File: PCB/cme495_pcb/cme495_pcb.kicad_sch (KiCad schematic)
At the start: 13 parts, among them J1 Conn_01x20_Socket, J2 Conn_01x20_Socket, J3 Conn_01x05_Socket, J4 Conn_01x05_Socket, J5 Conn_01x05_Socket, J6 Conn_01x05_Socket, J7 Conn_01x12_Socket, SW0 SW_Push_Open, SW1 SW_Push_Open, SW2 SW_Push_Open, SW3 SW_Push_Open, U1 MCP3208, U2 MCP3208

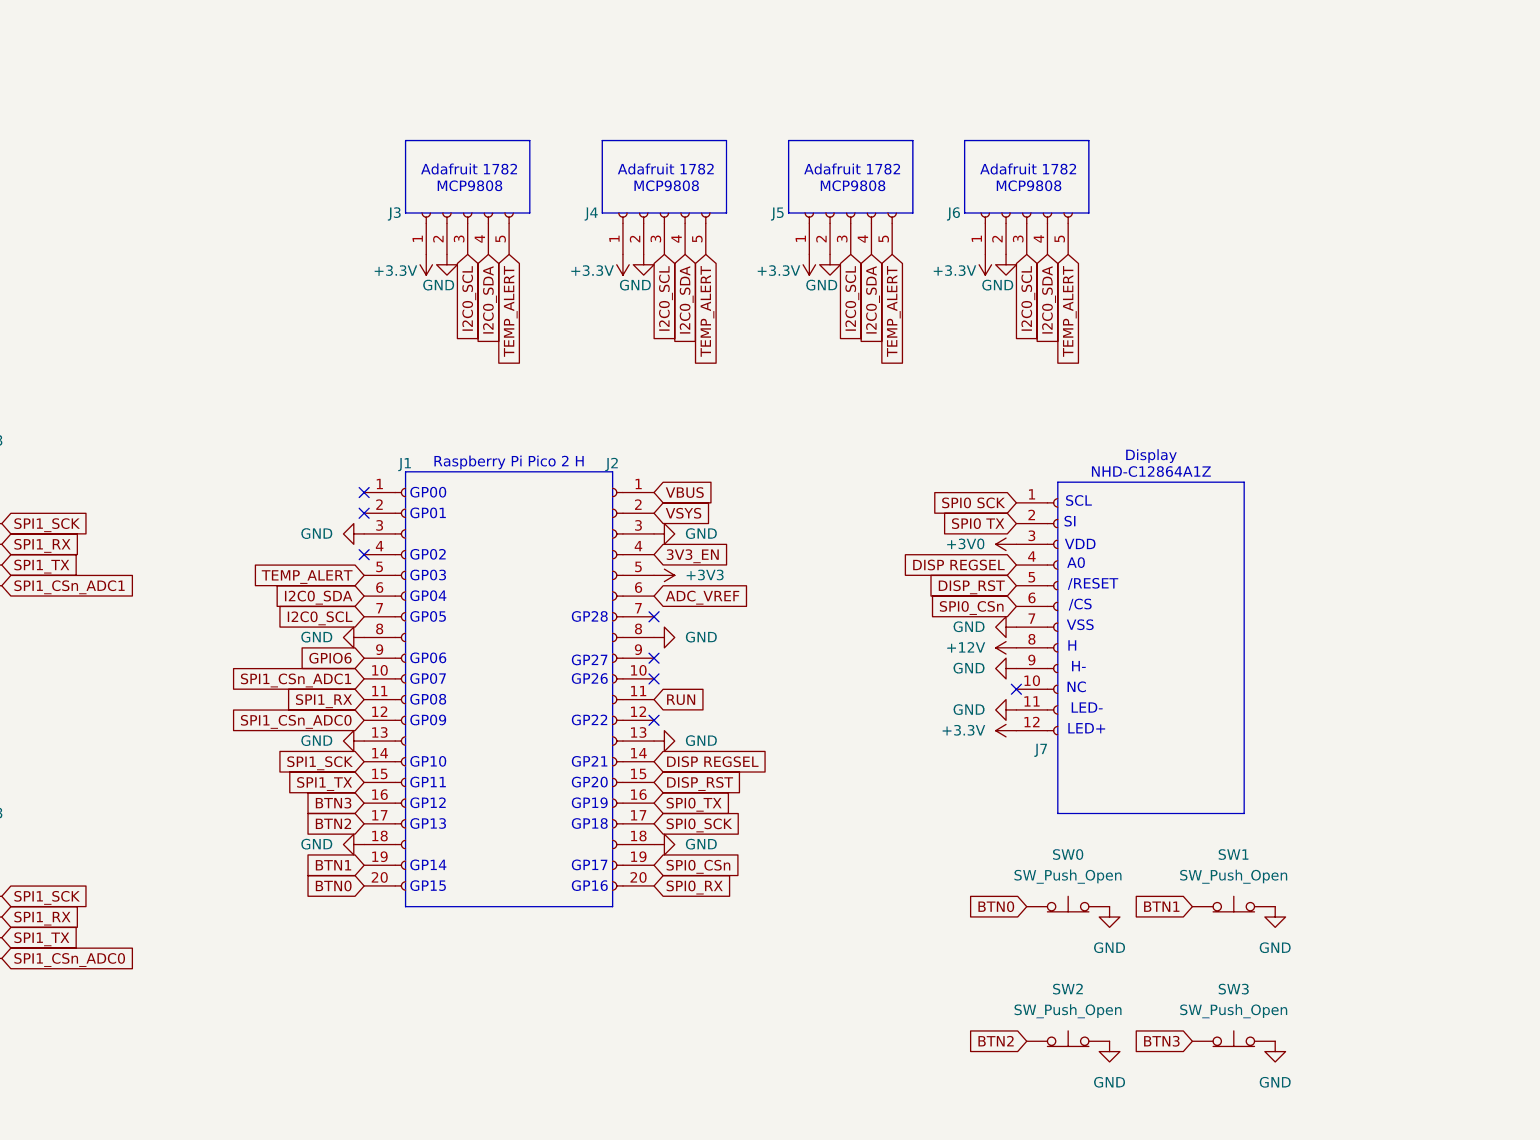
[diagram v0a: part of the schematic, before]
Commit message: added xh connector plans
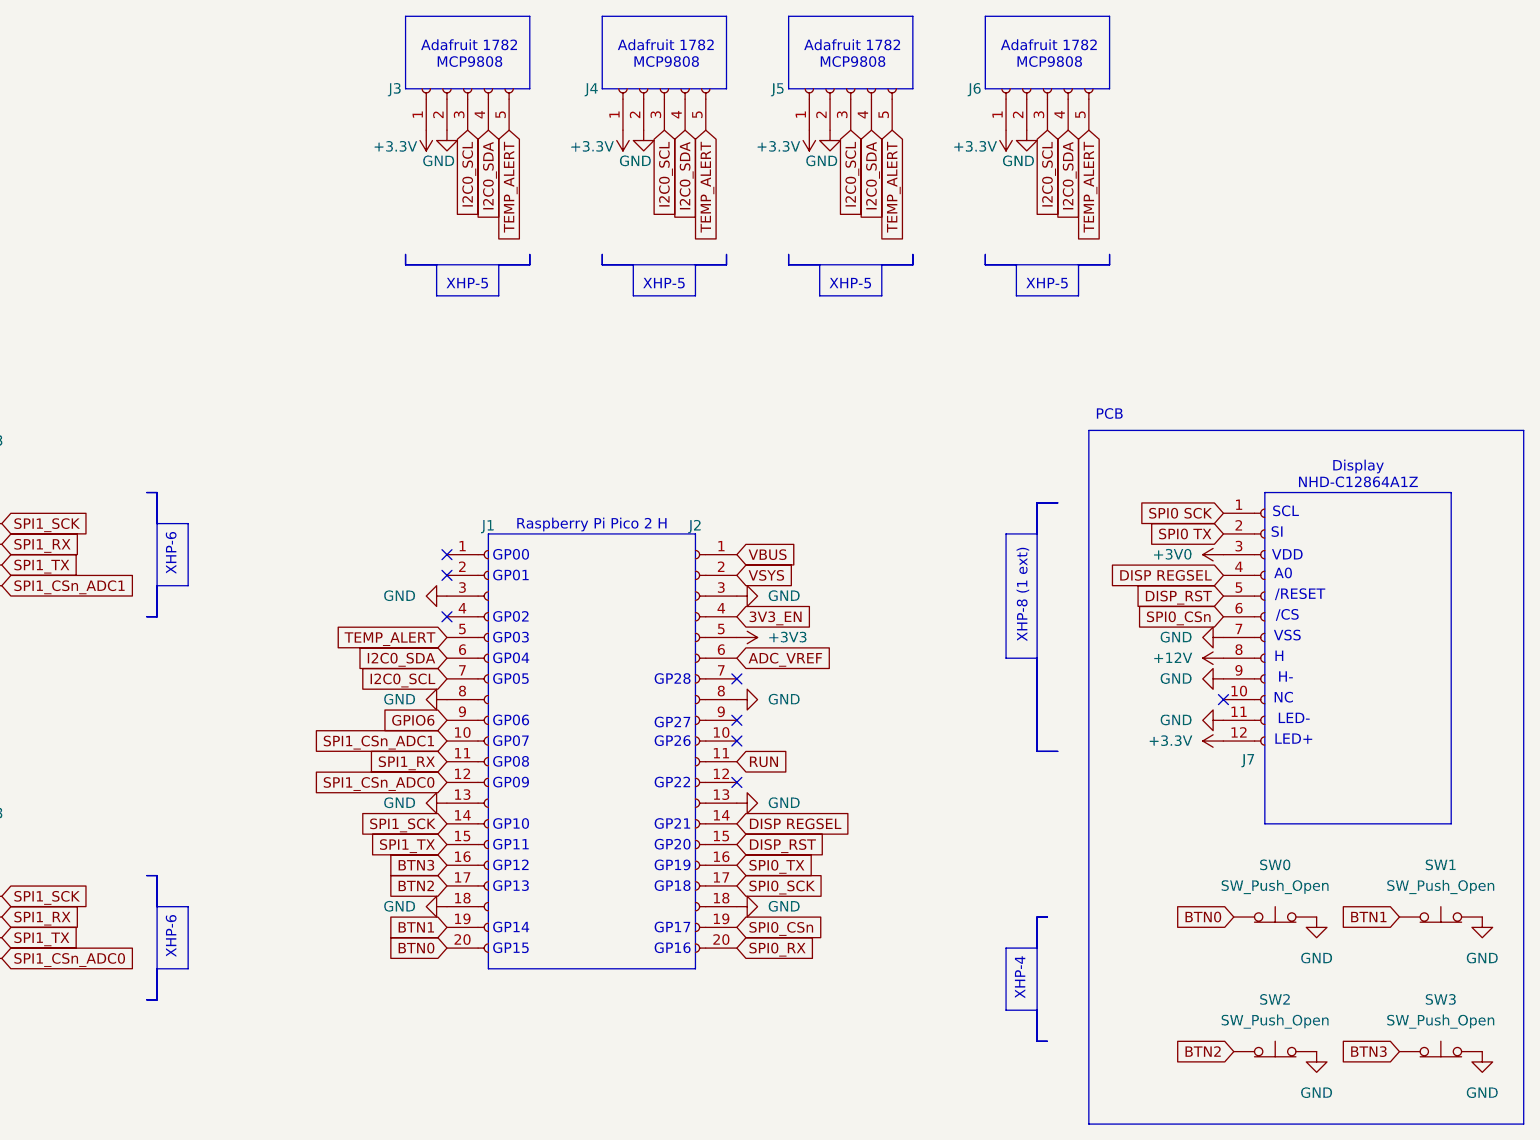
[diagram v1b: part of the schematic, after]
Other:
- note added: "PCB"
- note added: "XHP-4"
- note added: "XHP-5"
- note added: "XHP-6"
- note added: "XHP-8 (1 ext)"
- moved on the sheet: J1, J2, J3, J4, J5, J6, J7, SW0, SW1, SW2, SW3

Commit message: pins changed
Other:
- note added: "XHP-6 (+1)"
- note added: "XHP-8 (+1)"
- note removed: "XHP-5"
- note removed: "XHP-8 (1 ext)"
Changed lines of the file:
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@@
 		)
 	)
-	(text "XHP-5\n"
+	(text "XHP-6 (+1)\n"
 		(exclude_from_sim no)
 		(at 189.23 55.88 0)
@@
 		)
 	)
-	(text "XHP-5\n"
+	(text "XHP-6 (+1)\n"
 		(exclude_from_sim no)
 		(at 118.11 55.88 0)
@@
 		)
 	)
-	(text "XHP-5\n"
+	(text "XHP-6 (+1)\n"
 		(exclude_from_sim no)
 		(at 165.1 55.88 0)
@@
 		)
 	)
-	(text "XHP-5\n"
+	(text "XHP-6 (+1)\n"
 		(exclude_from_sim no)
 		(at 142.24 55.88 0)
@@
 		)
 	)
-	(text "XHP-8 (1 ext)\n\n"
-		(exclude_from_sim no)
-		(at 187.198 93.98 90)
-		(effects
-			(font
+	(text "XHP-8 (+1)"
+		(exclude_from_sim no)
+		(at 186.182 93.98 90)
+		(effects
+			(font

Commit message: Added KiCad parts to library for circuit layout.
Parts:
- removed J7: Conn_01x12_Socket, symbol Connector:Conn_01x12_Socket
- added C1, C10, C11, C12, C13, C14, C15, C16, C18, C19, C2, C3, C4, C5, C6, C7, C8, C9: C_Small, symbol Device:C_Small
- added F1, F2: Fuse, symbol Device:Fuse
- added J8 (x2): Conn_01x07_Socket, symbol Connector:Conn_01x07_Socket
- added L1, L2: L, symbol Device:L
- added Q2: IRLZ44N, Package_TO_SOT_THT:TO-220-3_Vertical, symbol Transistor_FET:IRLZ44N
- added R1, R2, R3, R4, R7, R8: R_Small_US, symbol Device:R_Small_US
- added SW4, SW5, SW6, SW7: SW_Push_Open, symbol Switch:SW_Push_Open
- added U3, U4: AP62300TWU, Package_TO_SOT_SMD:TSOT-23-6, symbol Regulator_Switching:AP62300TWU
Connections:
- net +12V: now also J8.7 (Pin_7)
- net +3.3V: now also J8.4 (Pin_4), J8.6 (Pin_6)
- net BTN0: now also SW4.1 (A)
- net BTN1: now also SW6.1 (A)
- net BTN2: now also SW5.1 (A)
- net BTN3: now also SW7.1 (A)
- net DISP REGSEL: now also J8.5 (Pin_5)
- net DISP_RST: now also J8.6 (Pin_6)
- net GND: now also C1.1, C1.2, C10.1, C11.1, C11.2, C12.1, C12.2, C13.1, C13.2, C14.2, C15.2, C16.1, C16.2, C18.2, C19.2, C2.2, C5.2, C6.2, C7.2, C9.1, C9.2, F1.1, F1.2, F2.1, J8.1 (Pin_1), J8.1 (Pin_1), J8.3 (Pin_3), J8.4 (Pin_4), J8.5 (Pin_5), L2.2, Q2.3 (S), R2.2, R3.1, R4.2, R8.2, SW4.2 (B), SW5.2 (B), SW6.2 (B), SW7.2 (B), U3.1 (GND), U4.1 (GND)
- net SPI0 SCK: now also J8.2 (Pin_2)
- net SPI0 TX: now also J8.3 (Pin_3)
- net SPI0_CSn: now also J8.7 (Pin_7)
- net HEATER_ON: now reaches J2.12 (Pin_12)
- new net: Q2.1 (G), R7.1, R8.1
- new net: C4.2, R1.2, R2.1, U4.4 (FB)
- new net: C8.2, L2.1, U3.2 (SW)
- new net: C10.2, R3.2, R4.1, U3.4 (FB)
- new net: C8.1, U3.6 (BST)
- new net: C2.1, F2.2, U4.3 (IN), U4.5 (EN)
- new net: C3.2, L1.1, U4.2 (SW)
- new net: C3.1, U4.6 (BST)
- new net Vout: C14.1, C15.1, C18.1, C19.1, C4.1, C5.1, C6.1, C7.1, L1.2, R1.1, U3.3 (IN), U3.5 (EN)
- new net heater_actuation_signal: R7.2
- no-connect marks 14 -> 13
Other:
- note added: "1-2A Fuse"
- note added: "100"
- note added: "100k"
- note added: "100n"
- note added: "100p"
- note added: "10k"
- note added: "10u"
- note added: "12Ω power resistor"
- note added: "22u"
- note added: "3.3V"
- note added: "3.3u"
- note added: "33.2k"
- note added: "56.2k"
- note added: "5V"
- note added: "8A Fuse"
- note added: "ADC modules"
- note added: "A_COMMON"
- note added: "CS"
- note added: "D"
- note added: "Fans"
- note added: "G"
- note added: "H+"
- note added: "K_B"
- note added: "K_G"
- note added: "K_R"
- note added: "LCD"
- note added: "RESET"
- note added: "S"
- note added: "Typical 14.4V, Max 16.8V, Min 12V"
- note added: "based on output from temp sensors & uC logic"
- note added: "battery protection module"
- note added: "buck converter for 12V->5V"
- note added: "buck converter for 5V->3.3V"
- note added: "heater"
- note added: "opamps for analog circuits"
- note added: "photodiodes"
- note added: "temp sensors"
- note added: "uC"
- note removed: "/CS"
- note removed: "/RESET"
- note removed: "H"
- note removed: "LED+"
- note removed: "LED-"
- moved on the sheet: SW0, SW1, SW2, SW3, U1, U2
